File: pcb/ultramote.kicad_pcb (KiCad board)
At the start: 2 copper layers, 40 x 42.5 mm, 58 parts, among them J1 SMA-KWE902, J2 SM02B-SRSS-TB, J3 USB-C-XKB_U262-16XN, J5 WST-REDFIT-4P, J6 PJ-242D-SMT, J7 PJ-242D-SMT, Q1 2N7002, Q2 BSS84, SW1 SSSS211603, U1 LoRa-E5, U2 TPS2112APW, U3 MCP73831-5-OT, U4 TLV70233DBVT, U5 CH340N, U6 EL357, U7 EL357

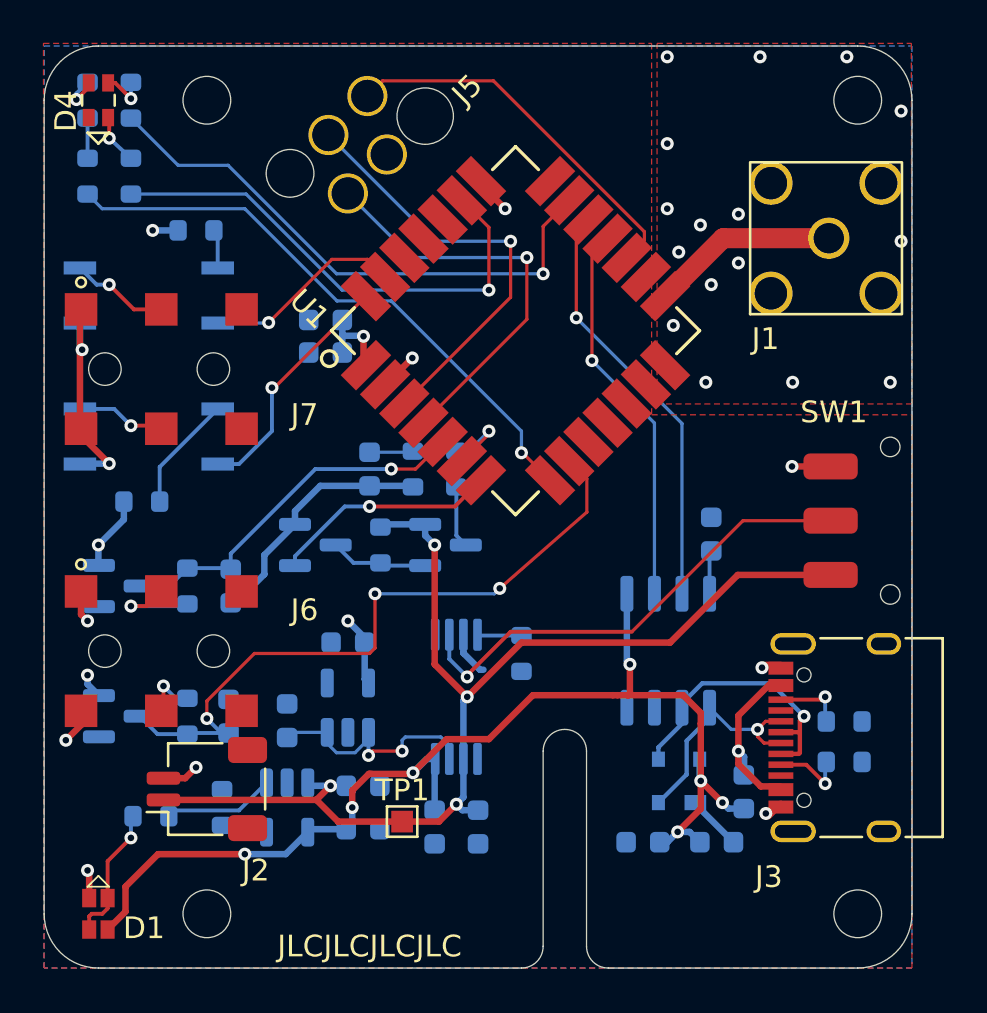
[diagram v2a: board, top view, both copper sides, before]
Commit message: Fix Pin Assignment for Output jack
closes #4
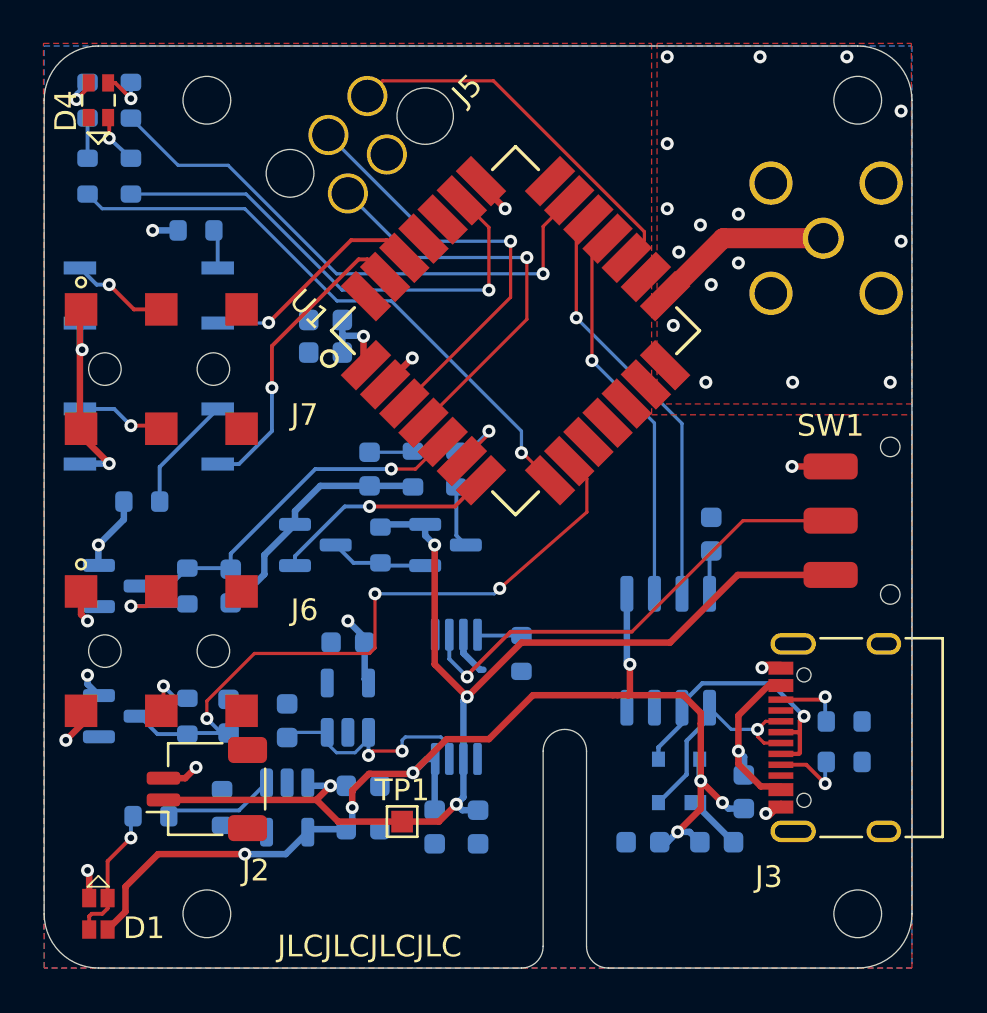
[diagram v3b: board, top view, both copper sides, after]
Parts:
- J1: moved to B.Cu
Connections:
- U1 pad 26: unconnected-(U1-PB14-Pad26) -> /OUTPUT_SLEEVE
- U1 pad 27: /OUTPUT_SLEEVE -> /OUTPUT_TIP
- U1 pad 28: /OUTPUT_TIP -> unconnected-(U1-PB0-Pad28)
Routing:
- net /OUTPUT_TIP: track 11.2 -> 14.3 mm
- net /OUTPUT_SLEEVE: track 9.27 -> 10.5 mm
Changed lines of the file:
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@@
   (net 59 "unconnected-(U1-PB13~{}-Pad24)")
   (net 60 "unconnected-(U1-PB9-Pad25)")
-  (net 61 "unconnected-(U1-PB14-Pad26)")
+  (net 61 "unconnected-(U1-PB0-Pad28)")
   (net 62 "unconnected-(U2-STAT-Pad1)")
   (net 63 "unconnected-(U4-NC-Pad4)")
@@
     )
   )
-  (footprint "ultramote:SMA-KWE902" (layer "F.Cu")
-    (at 123.54 65.86 90)
-    (property "LCSC Part Number" "C914554")
-    (property "Manufacturer Part Number" "SMA-KE-P903")
-    (property "Sheetfile" "ultramote.kicad_sch")
-    (property "Sheetname" "")
-    (property "ki_description" "coaxial connector (BNC, SMA, SMB, SMC, Cinch/RCA, LEMO, ...)")
-    (property "ki_keywords" "BNC SMA SMB SMC LEMO coaxial connector CINCH RCA")
-    (attr through_hole)
-    (fp_text reference "J1" (at -4.64 -2.79 unlocked) (layer "F.SilkS")
-        (effects (font (size 1 1) (thickness 0.15)))
-    )
-    (fp_text value "SMA-KWE902" (at -13.5 11.5 90 unlocked) (layer "F.Fab")
-        (effects (font (size 1 1) (thickness 0.15)))
-    )
-    (fp_text user "${REFERENCE}" (at 9 8 90 unlocked) (layer "F.Fab")
-        (effects (font (size 1 1) (thickness 0.15)))
-    )
-    (fp_rect (start -3.5 -3.5) (end 3.5 3.5)
-      (stroke (width 0.12) (type default)) (fill none) (layer "F.SilkS"))
-    (pad "1" thru_hole circle (at 0 0.127 90) (size 1.9 1.9) (drill 1.4) (layers "*.Cu" "*.Mask")
-      (net 20 "Net-(J1-In)") (pinfunction "In") (pintype "passive"))
-    (pad "2" thru_hole circle (at -2.54 -2.54 90) (size 2 2) (drill 1.5) (layers "*.Cu" "*.Mask")
-      (net 2 "GND") (pinfunction "Ext") (pintype "passive"))
-    (pad "2" thru_hole circle (at -2.54 2.54 90) (size 2 2) (drill 1.5) (layers "*.Cu" "*.Mask")
-      (net 2 "GND") (pinfunction "Ext") (pintype "passive"))
-    (pad "2" thru_hole circle (at 2.54 -2.54 90) (size 2 2) (drill 1.5) (layers "*.Cu" "*.Mask")
-      (net 2 "GND") (pinfunction "Ext") (pintype "passive"))
-    (pad "2" thru_hole circle (at 2.54 2.54 90) (size 2 2) (drill 1.5) (layers "*.Cu" "*.Mask")
-      (net 2 "GND") (pinfunction "Ext") (pintype "passive"))
-  )
   (footprint "MountingHole:MountingHole_2.2mm_M2" (layer "F.Cu")
     (at 95 97)
@@
       (net 60 "unconnected-(U1-PB9-Pad25)") (pinfunction "PB9") (pintype "bidirectional+no_connect"))
     (pad "26" smd rect (at -1.25 -6 45) (size 1 2.3) (layers "F.Cu" "F.Paste" "F.Mask")
-      (net 61 "unconnected-(U1-PB14-Pad26)") (pinfunction "PB14") (pintype "bidirectional+no_connect"))
+      (net 48 "/OUTPUT_SLEEVE") (pinfunction "PB14") (pintype "bidirectional"))
     (pad "27" smd rect (at -2.5 -6 45) (size 1 2.3) (layers "F.Cu" "F.Paste" "F.Mask")
-      (net 48 "/OUTPUT_SLEEVE") (pinfunction "PA10") (pintype "bidirectional"))
+      (net 49 "/OUTPUT_TIP") (pinfunction "PA10") (pintype "bidirectional"))
     (pad "28" smd rect (at -3.75 -6 45) (size 1 2.3) (layers "F.Cu" "F.Paste" "F.Mask")
-      (net 49 "/OUTPUT_TIP") (pinfunction "PB0") (pintype "bidirectional"))
+      (net 61 "unconnected-(U1-PB0-Pad28)") (pinfunction "PB0") (pintype "bidirectional"))
     (model "${KIPRJMOD}/cad_models/lorae5.STEP"
       (offset (xyz 0.08 1.4 0.5))
@@
     (property "ki_keywords" "switch single-pole double-throw spdt ON-ON")
     (attr smd)
-    (fp_text reference "SW1" (at -5 2.6 unlocked) (layer "F.SilkS")
+    (fp_text reference "SW1" (at -4.38 2.75 unlocked) (layer "F.SilkS")
         (effects (font (size 1 1) (thickness 0.15)))
     )
@@
     )
   )
+  (footprint "ultramote:SMA-KWE902" (layer "B.Cu")
+    (at 123.54 65.86 90)
+    (property "LCSC Part Number" "C914554")
+    (property "Manufacturer Part Number" "SMA-KE-P903")
+    (property "Sheetfile" "ultramote.kicad_sch")
+    (property "Sheetname" "")
+    (property "ki_description" "coaxial connector (BNC, SMA, SMB, SMC, Cinch/RCA, LEMO, ...)")
+    (property "ki_keywords" "BNC SMA SMB SMC LEMO coaxial connector CINCH RCA")
+    (attr through_hole)
+    (fp_text reference "J1" (at -4.64 -3.04 unlocked) (layer "B.SilkS")
+        (effects (font (size 1 1) (thickness 0.15)) (justify mirror))
+    )
+    (fp_text value "SMA-KWE902" (at -13.5 -11.5 270 unlocked) (layer "B.Fab")
+        (effects (font (size 1 1) (thickness 0.15)) (justify mirror))
+    )
+    (fp_text user "${REFERENCE}" (at 9 -8 270 unlocked) (layer "B.Fab")
+        (effects (font (size 1 1) (thickness 0.15)) (justify mirror))
+    )
+    (fp_rect (start -3.5 3.5) (end 3.5 -3.5)
+      (stroke (width 0.12) (type default)) (fill none) (layer "B.SilkS"))
+    (pad "1" thru_hole circle (at 0 -0.127 90) (size 1.9 1.9) (drill 1.4) (layers "*.Cu" "*.Mask")
+      (net 20 "Net-(J1-In)") (pinfunction "In") (pintype "passive"))
+    (pad "2" thru_hole circle (at -2.54 -2.54 90) (size 2 2) (drill 1.5) (layers "*.Cu" "*.Mask")
+      (net 2 "GND") (pinfunction "Ext") (pintype "passive"))
+    (pad "2" thru_hole circle (at -2.54 2.54 90) (size 2 2) (drill 1.5) (layers "*.Cu" "*.Mask")
+      (net 2 "GND") (pinfunction "Ext") (pintype "passive"))
+    (pad "2" thru_hole circle (at 2.54 -2.54 90) (size 2 2) (drill 1.5) (layers "*.Cu" "*.Mask")
+      (net 2 "GND") (pinfunction "Ext") (pintype "passive"))
+    (pad "2" thru_hole circle (at 2.54 2.54 90) (size 2 2) (drill 1.5) (layers "*.Cu" "*.Mask")
+      (net 2 "GND") (pinfunction "Ext") (pintype "passive"))
+    (model "${KIPRJMOD}/cad_models/SMA ANGLED.STEP"
+      (offset (xyz 0 0 -3.85))
+      (scale (xyz 1 1 1))
+      (rotate (xyz 0 0 0))
+    )
+  )
   (footprint "Capacitor_SMD:C_0603_1608Metric" (layer "B.Cu")
     (at 115.1 93.7 180)
@@
   (segment (start 116.9 74.4) (end 116.9 82.25) (width 0.15) (layer "B.Cu") (net 47))
   (segment (start 112.028274 69.528274) (end 116.9 74.4) (width 0.15) (layer "B.Cu") (net 47))
-  (segment (start 103.216951 67.647767) (end 102.403778 66.834594) (width 0.15) (layer "F.Cu") (net 48))
-  (segment (start 102.403778 66.834594) (end 100.764908 66.834594) (width 0.15) (layer "F.Cu") (net 48))
-  (segment (start 100.764908 66.834594) (end 97.849502 69.75) (width 0.15) (layer "F.Cu") (net 48))
+  (segment (start 101.648791 65.950711) (end 103.287662 65.950711) (width 0.18) (layer "F.Cu") (net 48))
+  (segment (start 103.287662 65.950711) (end 104.100835 66.763884) (width 0.18) (layer "F.Cu") (net 48))
+  (segment (start 97.849502 69.75) (end 101.648791 65.950711) (width 0.18) (layer "F.Cu") (net 48))
   (via (at 97.849502 69.75) (size 0.6) (drill 0.3) (layers "F.Cu" "B.Cu") (net 48))
   (segment (start 97.829501 69.770001) (end 95.5 69.770001) (width 0.15) (layer "B.Cu") (net 48))
   (segment (start 97.849502 69.75) (end 97.829501 69.770001) (width 0.15) (layer "B.Cu") (net 48))
-  (segment (start 98.114719 72.75) (end 98 72.75) (width 0.15) (layer "F.Cu") (net 49))
-  (segment (start 102.333068 68.531651) (end 98.114719 72.75) (width 0.15) (layer "F.Cu") (net 49))
+  (segment (start 98 70.828251) (end 98 72.75) (width 0.18) (layer "F.Cu") (net 49))
+  (segment (start 102.403778 66.834594) (end 101.993657 66.834594) (width 0.18) (layer "F.Cu") (net 49))
+  (segment (start 103.216951 67.647767) (end 102.403778 66.834594) (width 0.18) (layer "F.Cu") (net 49))
+  (segment (start 101.993657 66.834594) (end 98 70.828251) (width 0.18) (layer "F.Cu") (net 49))
   (via (at 98 72.75) (size 0.6) (drill 0.3) (layers "F.Cu" "B.Cu") (net 49))
   (segment (start 95.5 76.270001) (end 96.479999 76.270001) (width 0.18) (layer "B.Cu") (net 49))

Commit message: Add QWIIC connector
closes #5
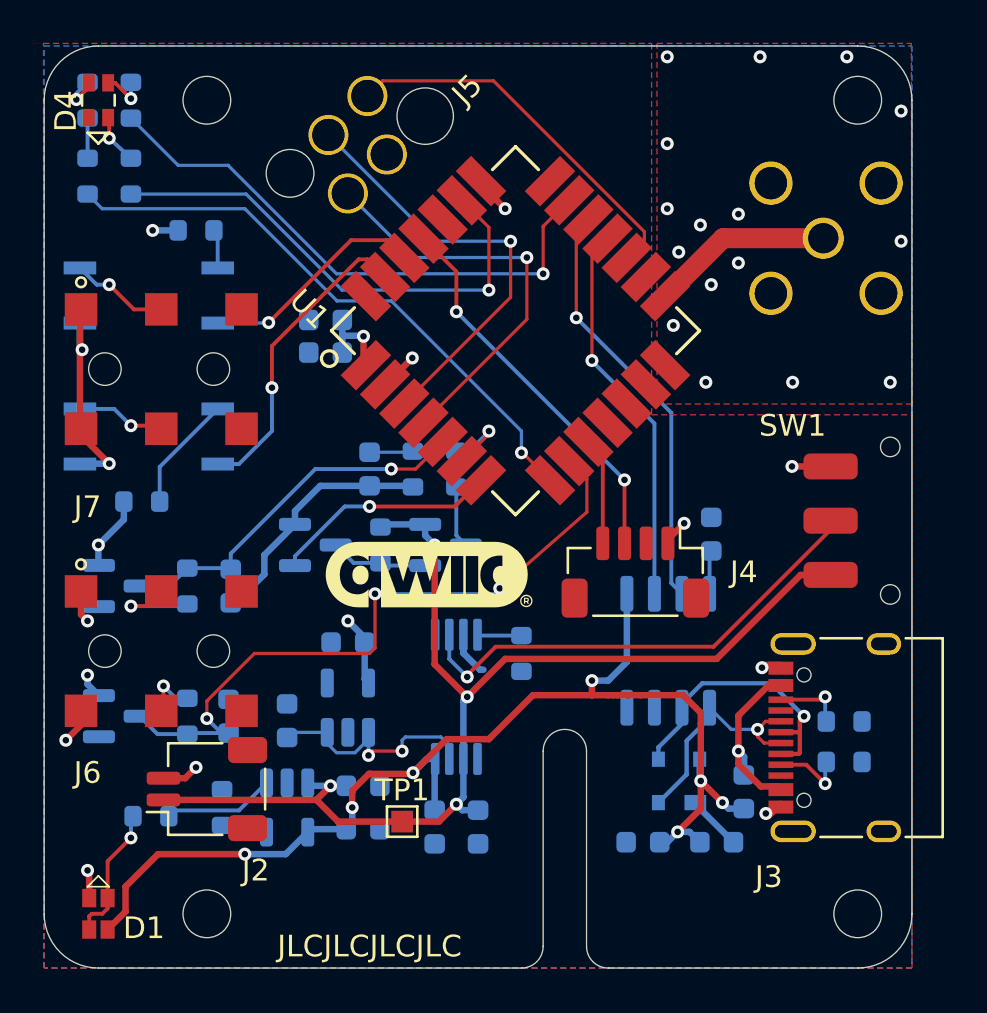
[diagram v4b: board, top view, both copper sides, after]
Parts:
- added J4: QWIIC, Connector_JST:JST_SH_BM04B-SRSS-TB_1x04-1MP_P1.00mm_Vertical, F.Cu at (114.8, 81.2)
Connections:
- U1 pad 10: unconnected-(U1-PB6-Pad10) -> /I2C_SCL
- U1 pad 25: unconnected-(U1-PB9-Pad25) -> /I2C_SDA
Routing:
- net /I2C_SDA: track 0.00 -> 17.9 mm, vias 0 -> 2
- net /I2C_SCL: track 0.00 -> 4.95 mm
- net GND: track 29.3 -> 30.5 mm, vias 25 -> 26
- net VBUS: track 53.5 -> 54.5 mm
